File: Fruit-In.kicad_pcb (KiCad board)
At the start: 2 copper layers, 69 parts, among them IC1 4N35, IC2 4N35, IC3 4N35, IC4 4N35, IC5 4N35, IC6 4N35, P1 CONN_1, P2 CONN_1, P3 CONN_1, P4 CONN_1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

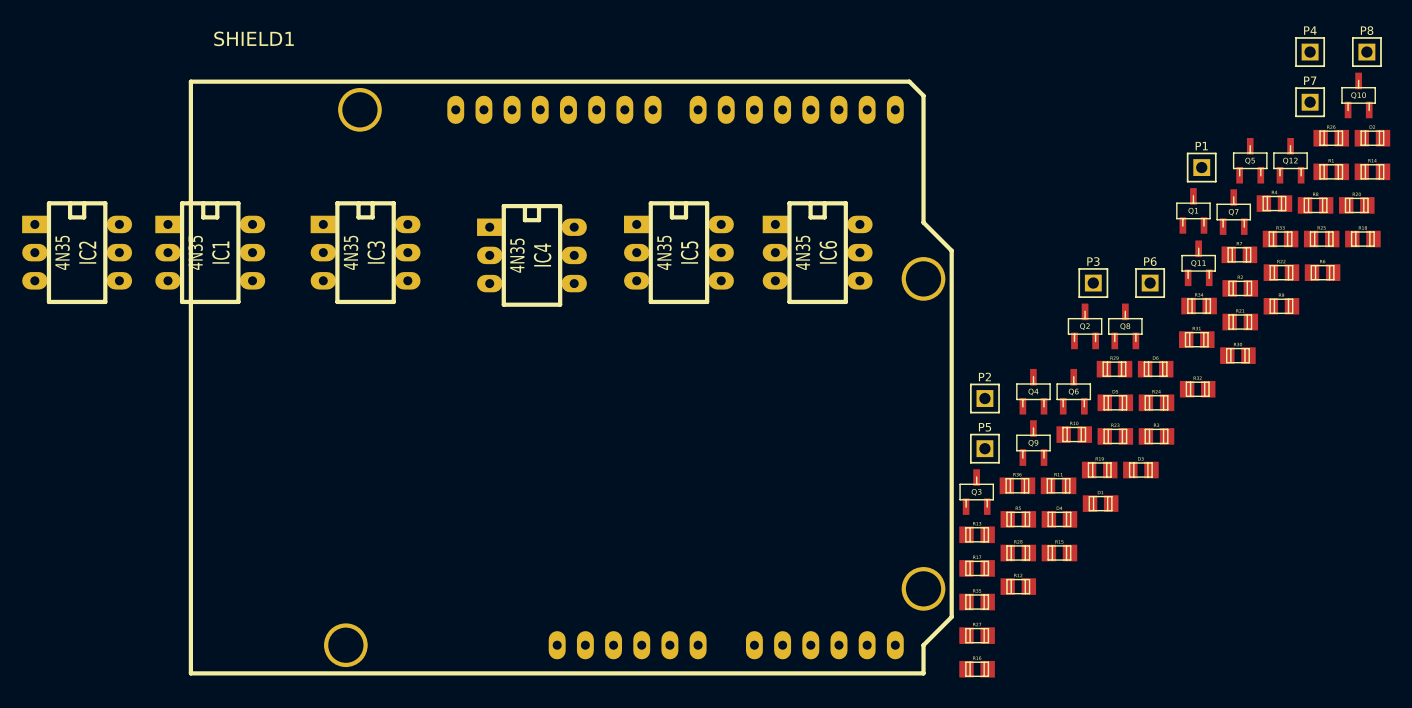
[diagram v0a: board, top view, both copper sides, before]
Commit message: Final version sent to OSH Park
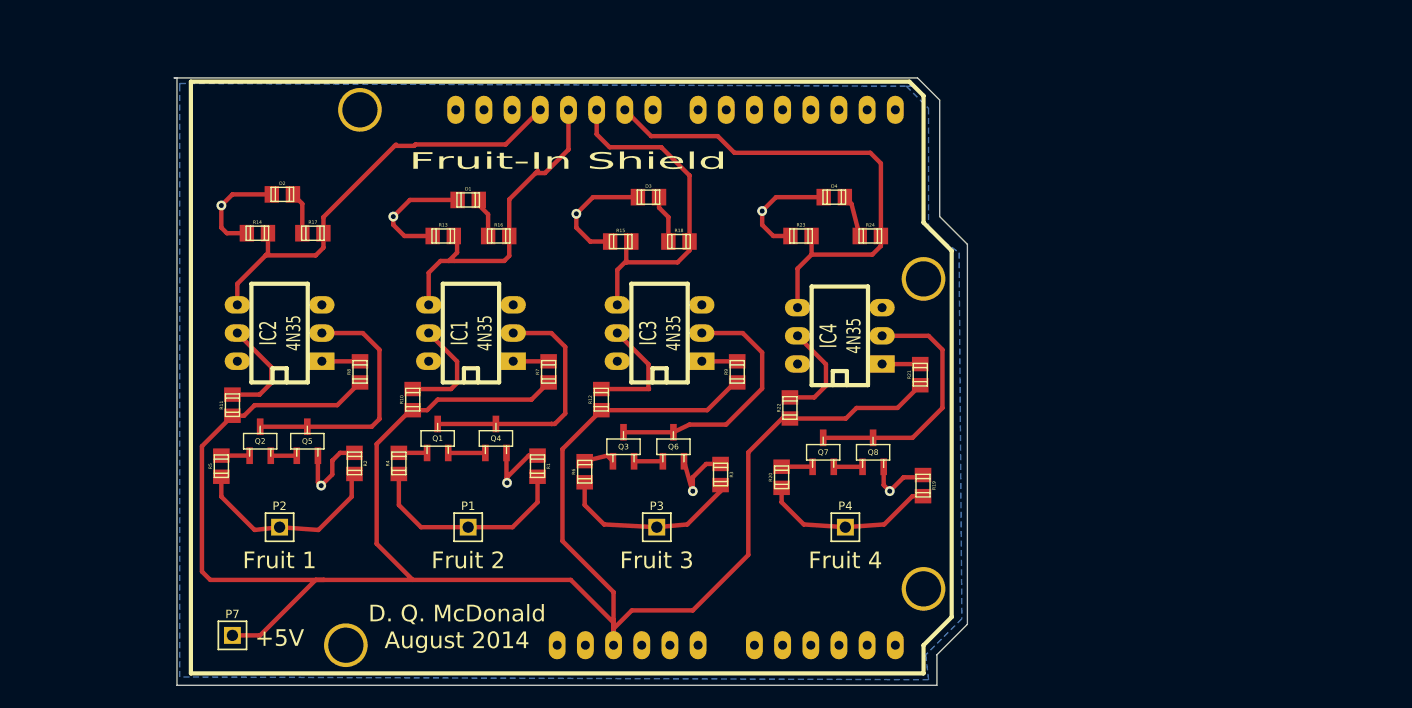
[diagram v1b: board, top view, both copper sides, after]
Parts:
- removed D5, D6: LED, smd_capacitors:c_0805
- removed IC5, IC6: 4N35, dip_sockets:DIP-6__300_ELL
- removed P5, P6, P8: CONN_1, pin_array:PIN_ARRAY_1
- removed Q10, Q11, Q12, Q9: 2N3904, DQM:sot23
- removed R25, R26: 2.2M, smd_capacitors:c_0805
- removed R27, R28, R33, R34: 10K, smd_capacitors:c_0805
- removed R29, R30, R31, R32: 220 Ohms, smd_capacitors:c_0805
- removed R35, R36: 470 Ohms, smd_capacitors:c_0805
- moved P7 108.4 mm to (53.8, 112.8)
- moved R14 100.7 mm to (56.0, 76.5)
- moved D2 98.4 mm to (58.2, 73.0)
- moved Q5 88.7 mm to (60.5, 95.2)
- moved R8 87.4 mm to (65.2, 89.0), turned to 90 degrees
- moved R4 82.3 mm to (68.8, 97.2), turned to 90 degrees
- moved R2 81.4 mm to (64.8, 97.2), turned to 270 degrees
- moved R1 76.3 mm to (81.2, 97.5), turned to 270 degrees
- moved Q2 75.1 mm to (56.2, 95.2)
- moved R11 74.8 mm to (53.8, 92.0), turned to 90 degrees
- moved P1 73.6 mm to (75.0, 103.0)
- moved R5 72.0 mm to (52.8, 97.5), turned to 90 degrees
- moved Q1 71.1 mm to (72.2, 95.0)
- moved R6 68.9 mm to (85.5, 98.0), turned to 90 degrees
- moved R17 67.1 mm to (61.0, 76.5)
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- renumbered SHIELD1 to ?
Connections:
- ? pad 7: D7 -> Net-(SHIELD1-Pad7)
- ? pad 8: D8 -> Net-(SHIELD1-Pad8)
- P7 pad 1: GND -> +5V
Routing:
- net +5V: track 0.00 -> 191.6 mm
- net GND: track 0.00 -> 69.7 mm, vias 0 -> 8
- net D9: track 0.00 -> 46.1 mm
- net D12: track 0.00 -> 39.6 mm
- net D10: track 0.00 -> 31.5 mm
- net D11: track 0.00 -> 29.6 mm
- net Net-(IC3-Pad2): track 0.00 -> 23.4 mm
- net Net-(IC1-Pad2): track 0.00 -> 23.2 mm
- net Net-(IC2-Pad2): track 0.00 -> 23.1 mm
- net Net-(IC4-Pad2): track 0.00 -> 23.1 mm
- net Net-(P1-Pad1): track 0.00 -> 19.4 mm
- net Net-(P2-Pad1): track 0.00 -> 18.2 mm
- net Net-(P3-Pad1): track 0.00 -> 16.8 mm
- net Net-(P4-Pad1): track 0.00 -> 15.9 mm
- net Net-(IC3-Pad5): track 0.00 -> 10.5 mm
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- added copper zone on B.Cu, net GND
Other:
- board outline added: 71.5 x 54.8 mm
- net class Default: trace_width 0.254 -> 0.4
- board text added: "+5V"
- board text added: "D. Q. McDonald August 2014"
- board text added: "Fruit 1"
- board text added: "Fruit 2"
- board text added: "Fruit 3"
- board text added: "Fruit 4"
- board text added: "Fruit-In Shield"
